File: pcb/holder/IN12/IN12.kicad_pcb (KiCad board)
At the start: 2 copper layers, 229.9 x 64.9 mm, 21 parts, among them J1 Conn_01x10, J2 Conn_01x10, J3 Conn_01x10, J4 Conn_01x10, J5 Conn_01x03, Q1 MPSA42, U1 NE555P

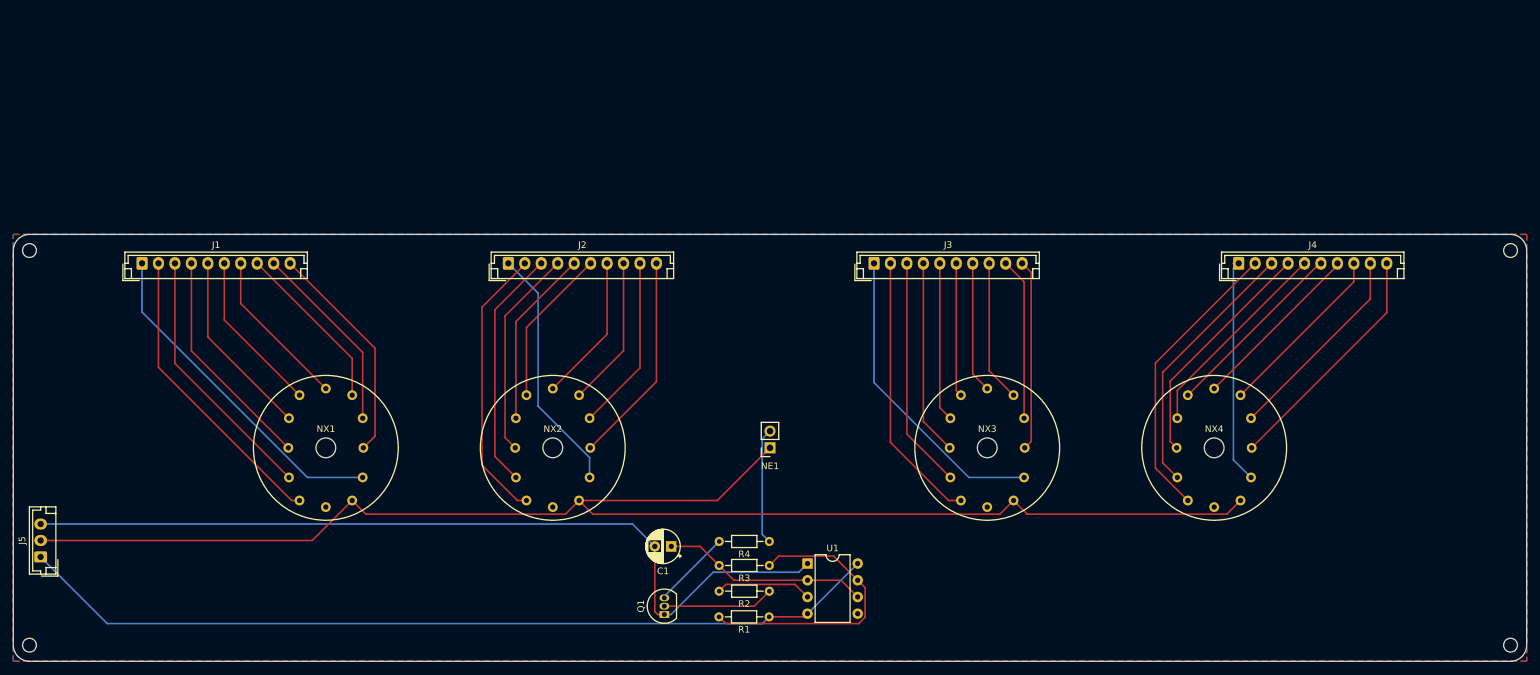
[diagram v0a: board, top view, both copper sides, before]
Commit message: Refactoring with 4-bit dynamic scan
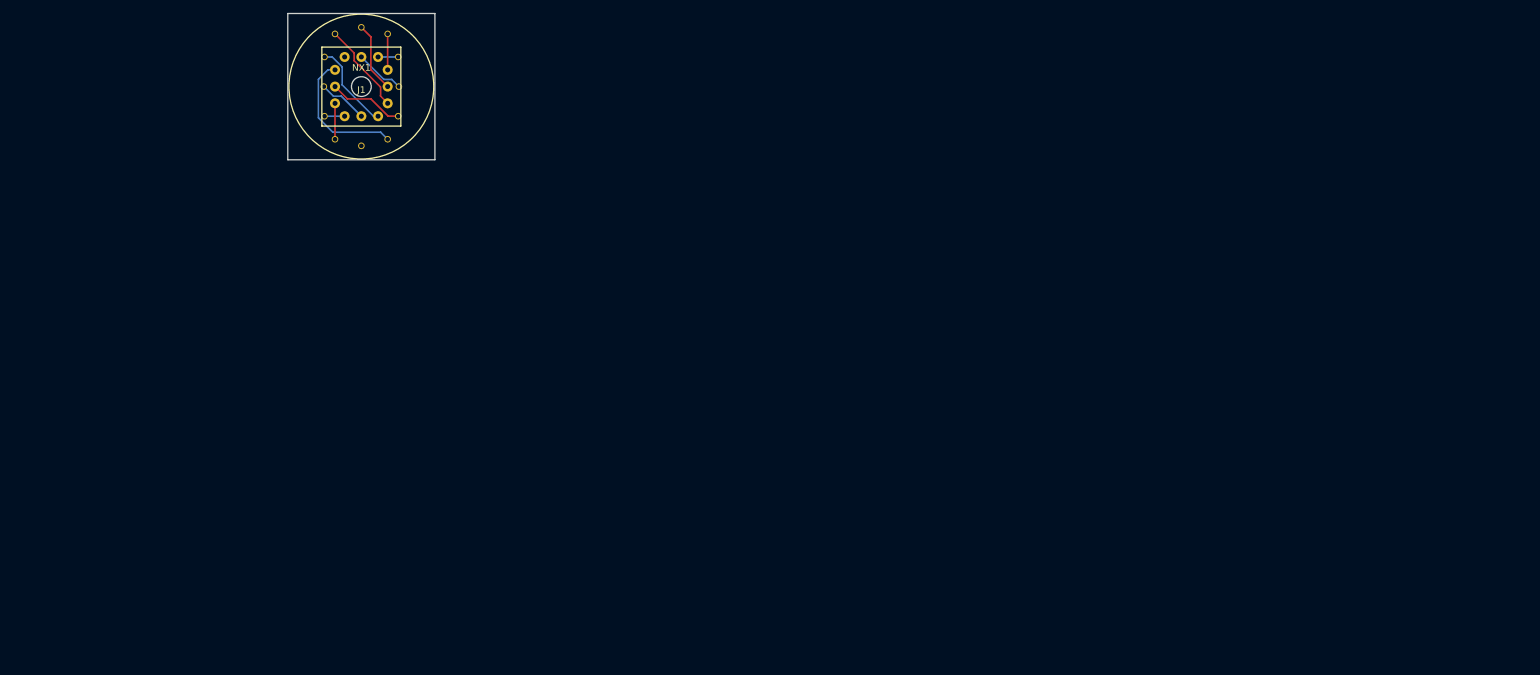
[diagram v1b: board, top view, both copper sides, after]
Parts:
- removed C1: 10uF, Capacitor_THT:CP_Radial_D5.0mm_P2.50mm
- removed J2, J3, J4: Conn_01x10, Connector_JST:JST_EH_B10B-EH-A_1x10_P2.50mm_Vertical
- removed J5: Conn_01x03, Connector_JST:JST_EH_B3B-EH-A_1x03_P2.50mm_Vertical
- removed NE1: Lamp_Neon, Connector_PinSocket_2.54mm:PinSocket_1x02_P2.54mm_Vertical
- removed NX2, NX3, NX4: IN-12A, Nixie_Clock:IN-12A
- removed Q1: MPSA42, Package_TO_SOT_THT:TO-92_Inline
- removed R1: 1k, Resistor_THT:R_Axial_DIN0204_L3.6mm_D1.6mm_P7.62mm_Horizontal
- removed R2: 10k, Resistor_THT:R_Axial_DIN0204_L3.6mm_D1.6mm_P7.62mm_Horizontal
- removed R3, R4: 100k, Resistor_THT:R_Axial_DIN0204_L3.6mm_D1.6mm_P7.62mm_Horizontal
- removed REF** (x4): MountingHole_2.1mm, MountingHole:MountingHole_2.1mm
- removed U1: NE555P, Package_DIP:DIP-8_W7.62mm
- J1: value Conn_01x10 -> Nixie_Conn_12P; footprint Connector_JST:JST_EH_B10B-EH-A_1x10_P2.50mm_Vertical -> Nixie_Clock:Nixie_Conn_12P
- moved NX1 55.1 mm to (147.3, 99.5)
- moved J1 42.8 mm to (147.3, 99.5)
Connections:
- J1 pad 1: Net-(J1-Pad1) -> P1
- J1 pad 10: Net-(J1-Pad10) -> unconnected-(J1-Pad10)
- J1 pad 2: Net-(J1-Pad2) -> P2
- J1 pad 3: Net-(J1-Pad3) -> P3
- J1 pad 4: Net-(J1-Pad4) -> P4
- J1 pad 5: Net-(J1-Pad5) -> P5
- J1 pad 6: Net-(J1-Pad6) -> P6
- J1 pad 7: Net-(J1-Pad7) -> P7
- J1 pad 8: Net-(J1-Pad8) -> P8
- J1 pad 9: Net-(J1-Pad9) -> P9
- NX1 pad 0: Net-(J1-Pad1) -> P0
- NX1 pad 1: Net-(J1-Pad2) -> P1
- NX1 pad 2: Net-(J1-Pad3) -> P2
- NX1 pad 3: Net-(J1-Pad4) -> P3
- NX1 pad 4: Net-(J1-Pad5) -> P4
- NX1 pad 5: Net-(J1-Pad6) -> P5
- NX1 pad 6: Net-(J1-Pad7) -> P6
- NX1 pad 7: Net-(J1-Pad8) -> P7
- NX1 pad 8: Net-(J1-Pad9) -> P8
- NX1 pad 9: Net-(J1-Pad10) -> P9
- NX1 pad A: ANODE_PIN -> PA
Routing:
- net ANODE_PIN: track 222.3 -> 0.00 mm
- net +5V: track 132.1 -> 0.00 mm
- net GND: track 131.2 -> 0.00 mm
- net Net-(J1-Pad1): track 51.3 -> 0.00 mm
- net Net-(J3-Pad1): track 46.9 -> 0.00 mm
- net Net-(J1-Pad2): track 45.6 -> 0.00 mm
- net Net-(R1-Pad2): track 44.6 -> 0.00 mm
- net Net-(J4-Pad2): track 44.3 -> 0.00 mm
- net Net-(J2-Pad2): track 42.5 -> 0.00 mm
- net Net-(J3-Pad2): track 41.6 -> 0.00 mm
- net Net-(J4-Pad3): track 40.3 -> 0.00 mm
- net Net-(J1-Pad3): track 39.7 -> 0.00 mm
- net Net-(J2-Pad1): track 38.1 -> 0.00 mm
- net Net-(J2-Pad3): track 36.8 -> 0.00 mm
- net Net-(J4-Pad10): track 36.5 -> 0.00 mm
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- removed copper zone on B.Cu, net GND
- removed copper zone on F.Cu, net GND
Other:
- board size 229.9 x 64.9 mm -> 22.4 x 22.2 mm
- net class Default removed

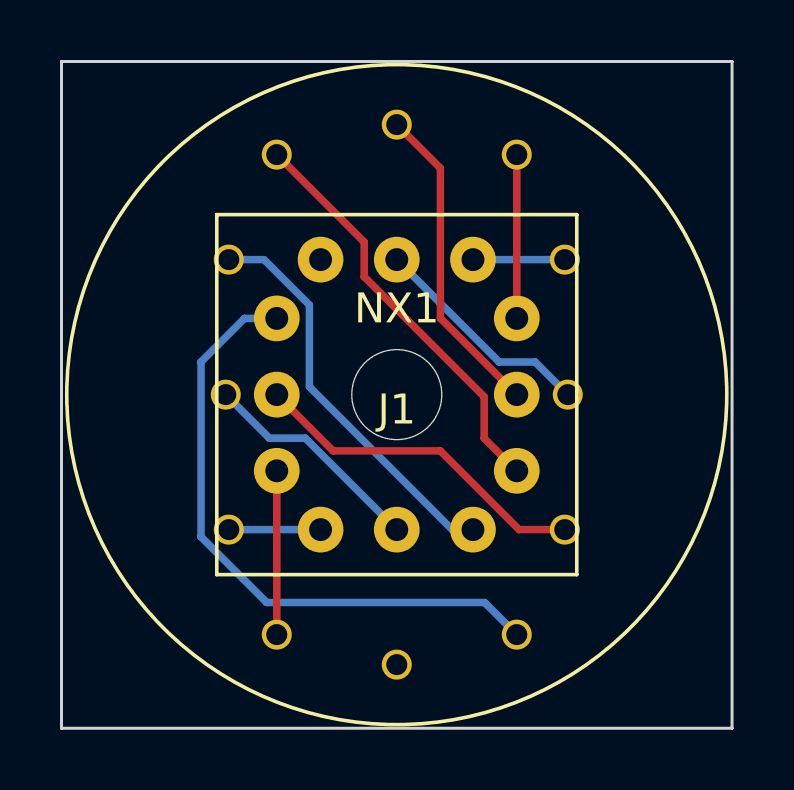
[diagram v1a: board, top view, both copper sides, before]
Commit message: Fix typo on nixie segment
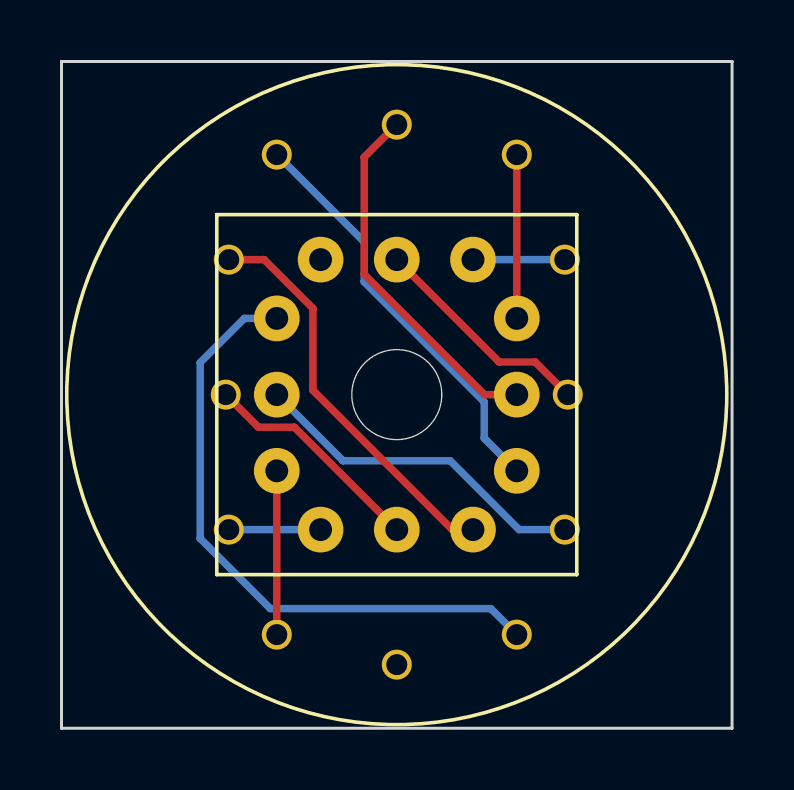
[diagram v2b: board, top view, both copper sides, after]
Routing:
- net P6: track 10.7 -> 12.2 mm
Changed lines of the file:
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@@
   )
   (setup
+    (stackup
+      (layer "F.SilkS" (type "Top Silk Screen"))
+      (layer "F.Paste" (type "Top Solder Paste"))
+      (layer "F.Mask" (type "Top Solder Mask") (thickness 0.01))
+      (layer "F.Cu" (type "copper") (thickness 0.035))
+      (layer "dielectric 1" (type "core") (thickness 1.51) (material "FR4") (epsilon_r 4.5) (loss_tangent 0.02))
+      (layer "B.Cu" (type "copper") (thickness 0.035))
+      (layer "B.Mask" (type "Bottom Solder Mask") (thickness 0.01))
+      (layer "B.Paste" (type "Bottom Solder Paste"))
+      (layer "B.SilkS" (type "Bottom Silk Screen"))
+      (copper_finish "None")
+      (dielectric_constraints no)
+    )
     (pad_to_mask_clearance 0)
     (pcbplotparams
@@
     (property "Sheetname" "")
     (attr through_hole)
-    (fp_text reference "J1" (at 0 0.5) (layer "F.SilkS")
+    (fp_text reference "J1" (at 0 0.5) (layer "F.SilkS") hide
         (effects (font (size 1 1) (thickness 0.15)))
     )
@@
     (property "Sheetname" "")
     (attr through_hole)
-    (fp_text reference "NX1" (at 0 -2.8702) (layer "F.SilkS")
+    (fp_text reference "NX1" (at 0 -2.8702) (layer "F.SilkS") hide
         (effects (font (size 1 1) (thickness 0.15)))
     )
@@
   (gr_rect (start 136.144 88.392) (end 158.496 110.617)
     (stroke (width 0.1) (type default)) (fill none) (layer "Edge.Cuts"))
-  (segment (start 151.397251 103.996) (end 148.772251 101.371) (width 0.25) (layer "F.Cu") (net 1))
-  (segment (start 148.772251 101.371) (end 145.195 101.371) (width 0.25) (layer "F.Cu") (net 1))
-  (segment (start 152.92 103.996) (end 151.397251 103.996) (width 0.25) (layer "F.Cu") (net 1))
-  (segment (start 145.195 101.371) (end 143.32 99.496) (width 0.25) (layer "F.Cu") (net 1))
+  (segment (start 149.102851 101.7016) (end 145.5256 101.7016) (width 0.25) (layer "B.Cu") (net 1))
+  (segment (start 145.5256 101.7016) (end 143.32 99.496) (width 0.25) (layer "B.Cu") (net 1))
+  (segment (start 152.92 103.996) (end 151.397251 103.996) (width 0.25) (layer "B.Cu") (net 1))
+  (segment (start 151.397251 103.996) (end 149.102851 101.7016) (width 0.25) (layer "B.Cu") (net 1))
   (segment (start 143.32 102.036) (end 143.32 107.496) (width 0.25) (layer "F.Cu") (net 2))
-  (segment (start 141.72 103.996) (end 144.78 103.996) (width 0.25) (layer "B.Cu") (net 3))
-  (segment (start 141.62 99.496) (end 143.073 100.949) (width 0.25) (layer "B.Cu") (net 4))
-  (segment (start 144.273 100.949) (end 147.32 103.996) (width 0.25) (layer "B.Cu") (net 4))
-  (segment (start 143.073 100.949) (end 144.273 100.949) (width 0.25) (layer "B.Cu") (net 4))
-  (segment (start 149.16835 103.996) (end 144.407 99.23465) (width 0.25) (layer "B.Cu") (net 5))
-  (segment (start 149.86 103.996) (end 149.16835 103.996) (width 0.25) (layer "B.Cu") (net 5))
-  (segment (start 144.407 96.505749) (end 142.897251 94.996) (width 0.25) (layer "B.Cu") (net 5))
-  (segment (start 144.407 99.23465) (end 144.407 96.505749) (width 0.25) (layer "B.Cu") (net 5))
-  (segment (start 142.897251 94.996) (end 141.72 94.996) (width 0.25) (layer "B.Cu") (net 5))
-  (segment (start 146.233 94.409) (end 146.233 95.568) (width 0.25) (layer "F.Cu") (net 6))
-  (segment (start 150.233 100.949) (end 151.32 102.036) (width 0.25) (layer "F.Cu") (net 6))
-  (segment (start 143.32 91.496) (end 146.233 94.409) (width 0.25) (layer "F.Cu") (net 6))
-  (segment (start 146.233 95.568) (end 150.233 99.568) (width 0.25) (layer "F.Cu") (net 6))
-  (segment (start 150.233 99.568) (end 150.233 100.949) (width 0.25) (layer "F.Cu") (net 6))
-  (segment (start 148.773 96.949) (end 148.773 91.949) (width 0.25) (layer "F.Cu") (net 7))
-  (segment (start 151.32 99.496) (end 148.773 96.949) (width 0.25) (layer "F.Cu") (net 7))
-  (segment (start 148.773 91.949) (end 147.32 90.496) (width 0.25) (layer "F.Cu") (net 7))
-  (segment (start 151.32 91.496) (end 151.32 96.956) (width 0.25) (layer "F.Cu") (net 8))
+  (segment (start 144.78 103.996) (end 141.72 103.996) (width 0.25) (layer "B.Cu") (net 3))
+  (segment (start 143.907 100.583) (end 142.707 100.583) (width 0.25) (layer "F.Cu") (net 4))
+  (segment (start 147.32 103.996) (end 143.907 100.583) (width 0.25) (layer "F.Cu") (net 4))
+  (segment (start 142.707 100.583) (end 141.62 99.496) (width 0.25) (layer "F.Cu") (net 4))
+  (segment (start 144.526 99.35365) (end 144.526 96.6216) (width 0.25) (layer "F.Cu") (net 5))
+  (segment (start 149.16835 103.996) (end 144.526 99.35365) (width 0.25) (layer "F.Cu") (net 5))
+  (segment (start 149.86 103.996) (end 149.16835 103.996) (width 0.25) (layer "F.Cu") (net 5))
+  (segment (start 144.526 96.6216) (end 142.9004 94.996) (width 0.25) (layer "F.Cu") (net 5))
+  (segment (start 142.9004 94.996) (end 141.72 94.996) (width 0.25) (layer "F.Cu") (net 5))
+  (segment (start 150.233 100.949) (end 151.32 102.036) (width 0.25) (layer "B.Cu") (net 6))
+  (segment (start 146.233 94.409) (end 146.233 95.7378) (width 0.25) (layer "B.Cu") (net 6))
+  (segment (start 143.32 91.496) (end 146.233 94.409) (width 0.25) (layer "B.Cu") (net 6))
+  (segment (start 150.233 99.7378) (end 150.233 100.949) (width 0.25) (layer "B.Cu") (net 6))
+  (segment (start 146.233 95.7378) (end 150.233 99.7378) (width 0.25) (layer "B.Cu") (net 6))
+  (segment (start 146.233 91.583) (end 147.32 90.496) (width 0.25) (layer "F.Cu") (net 7))
+  (segment (start 146.233 95.48663) (end 146.233 91.583) (width 0.25) (layer "F.Cu") (net 7))
+  (segment (start 150.24237 99.496) (end 146.233 95.48663) (width 0.25) (layer "F.Cu") (net 7))
+  (segment (start 151.32 99.496) (end 150.24237 99.496) (width 0.25) (layer "F.Cu") (net 7))
+  (segment (start 151.32 96.956) (end 151.32 91.496) (width 0.25) (layer "F.Cu") (net 8))
   (segment (start 149.86 94.996) (end 152.92 94.996) (width 0.25) (layer "B.Cu") (net 9))
-  (segment (start 151.933 98.409) (end 153.02 99.496) (width 0.25) (layer "B.Cu") (net 10))
-  (segment (start 150.733 98.409) (end 151.933 98.409) (width 0.25) (layer "B.Cu") (net 10))
-  (segment (start 147.32 94.996) (end 150.733 98.409) (width 0.25) (layer "B.Cu") (net 10))
-  (segment (start 140.795 104.237727) (end 142.983273 106.426) (width 0.25) (layer "B.Cu") (net 12))
-  (segment (start 142.24237 96.956) (end 140.795 98.40337) (width 0.25) (layer "B.Cu") (net 12))
-  (segment (start 140.795 98.40337) (end 140.795 104.237727) (width 0.25) (layer "B.Cu") (net 12))
+  (segment (start 150.733 98.409) (end 151.933 98.409) (width 0.25) (layer "F.Cu") (net 10))
+  (segment (start 151.933 98.409) (end 153.02 99.496) (width 0.25) (layer "F.Cu") (net 10))
+  (segment (start 147.32 94.996) (end 150.733 98.409) (width 0.25) (layer "F.Cu") (net 10))
+  (segment (start 140.7668 98.43157) (end 140.7668 104.2924) (width 0.25) (layer "B.Cu") (net 12))
+  (segment (start 142.24237 96.956) (end 140.7668 98.43157) (width 0.25) (layer "B.Cu") (net 12))
   (segment (start 143.32 96.956) (end 142.24237 96.956) (width 0.25) (layer "B.Cu") (net 12))
-  (segment (start 150.25 106.426) (end 151.32 107.496) (width 0.25) (layer "B.Cu") (net 12))
-  (segment (start 142.983273 106.426) (end 150.25 106.426) (width 0.25) (layer "B.Cu") (net 12))
+  (segment (start 150.4532 106.6292) (end 151.32 107.496) (width 0.25) (layer "B.Cu") (net 12))
+  (segment (start 143.1036 106.6292) (end 150.4532 106.6292) (width 0.25) (layer "B.Cu") (net 12))
+  (segment (start 140.7668 104.2924) (end 143.1036 106.6292) (width 0.25) (layer "B.Cu") (net 12))
 )
